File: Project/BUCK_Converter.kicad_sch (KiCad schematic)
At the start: 17 parts, among them J601 Screw_Terminal_01x04, U601 MAX15062AATA+T

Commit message: More files cleanup
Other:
- company: Quasi Peak -> ${COMPANY}
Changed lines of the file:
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@@
     (title "TMC6200-TA-T Eval Board")
     (date "2021-09-03")
-    (rev "ED A0")
-    (company "Quasi Peak")
+    (rev "${REVISION}")
+    (company "${COMPANY}")
+    (comment 1 "${ENGINEER}")
+    (comment 2 "${PHONE_NUMBER}")
+    (comment 3 "${EMAIL}")
+    (comment 4 "${SENTENCE}")
   )
   (junction (at 221.615 80.01) (diameter 0) (color 0 0 0 0)
@@
     (pin "1")
   )
-  (symbol (lib_id "Device:R") (at 168.91 111.76 0) (mirror x)
+  (symbol (lib_id "Device:R") (at 168.91 111.76 0) (mirror x) (unit 1)
     (in_bom yes) (on_board yes)
     (property "Reference" "R603" (id 0) (at 163.195 109.855 0)
@@
     (pin "2")
   )
-  (symbol (lib_id "Device:R") (at 152.4 84.455 0) (mirror x)
+  (symbol (lib_id "Device:R") (at 152.4 84.455 0) (mirror x) (unit 1)
     (in_bom yes) (on_board yes)
     (property "Reference" "R601" (id 0) (at 146.685 82.55 0)
@@
     (pin "2")
   )
-  (symbol (lib_id "Device:R") (at 152.4 93.345 0) (mirror x)
+  (symbol (lib_id "Device:R") (at 152.4 93.345 0) (mirror x) (unit 1)
     (in_bom yes) (on_board yes)
     (property "Reference" "R602" (id 0) (at 146.685 91.44 0)
@@
     (pin "2")
   )
-  (symbol (lib_id "Device:LED") (at 38.1 161.925 90)
+  (symbol (lib_id "Device:LED") (at 38.1 161.925 90) (unit 1)
     (in_bom yes) (on_board yes)
     (property "Reference" "D602" (id 0) (at 32.385 160.655 90)
@@
     (pin "2")
   )
-  (symbol (lib_id "Device:LED") (at 50.8 161.925 90)
+  (symbol (lib_id "Device:LED") (at 50.8 161.925 90) (unit 1)
     (in_bom yes) (on_board yes)
     (property "Reference" "D603" (id 0) (at 45.085 160.655 90)
@@
     (pin "2")
   )
-  (symbol (lib_id "Device:R") (at 38.1 153.035 0) (mirror x)
+  (symbol (lib_id "Device:R") (at 38.1 153.035 0) (mirror x) (unit 1)
     (in_bom yes) (on_board yes)
     (property "Reference" "R605" (id 0) (at 32.385 151.13 0)
@@
     (pin "2")
   )
-  (symbol (lib_id "Device:R") (at 25.4 153.035 0) (mirror x)
+  (symbol (lib_id "Device:R") (at 25.4 153.035 0) (mirror x) (unit 1)
     (in_bom yes) (on_board yes)
     (property "Reference" "R604" (id 0) (at 19.685 151.13 0)
@@
     (pin "2")
   )
-  (symbol (lib_id "Device:R") (at 50.8 153.035 0) (mirror x)
+  (symbol (lib_id "Device:R") (at 50.8 153.035 0) (mirror x) (unit 1)
     (in_bom yes) (on_board yes)
     (property "Reference" "R606" (id 0) (at 45.085 151.13 0)
@@
     (pin "1")
   )
-  (symbol (lib_id "eval_board_tmc6200-ta-rescue:MAX15062BATA+T-eval_board_tmc6200-ta") (at 167.005 77.47 0)
+  (symbol (lib_id "eval_board_tmc6200-ta-rescue:MAX15062BATA+T-eval_board_tmc6200-ta") (at 167.005 77.47 0) (unit 1)
     (in_bom yes) (on_board yes)
     (property "Reference" "U601" (id 0) (at 167.005 76.2 0)
@@
     (pin "1")
   )
-  (symbol (lib_id "Device:C") (at 142.875 89.535 0)
+  (symbol (lib_id "Device:C") (at 142.875 89.535 0) (unit 1)
     (in_bom yes) (on_board yes)
     (property "Reference" "C603" (id 0) (at 137.16 87.63 0)
@@
     (pin "2")
   )
-  (symbol (lib_id "Device:C") (at 120.65 89.535 0)
+  (symbol (lib_id "Device:C") (at 120.65 89.535 0) (unit 1)
     (in_bom yes) (on_board yes)
     (property "Reference" "C602" (id 0) (at 114.935 87.63 0)
@@
     (pin "1")
   )
-  (symbol (lib_id "Device:C") (at 204.47 98.425 0)
+  (symbol (lib_id "Device:C") (at 204.47 98.425 0) (unit 1)
     (in_bom yes) (on_board yes)
     (property "Reference" "C604" (id 0) (at 198.755 96.52 0)
@@
     (pin "1")
   )
-  (symbol (lib_id "Device:C") (at 221.615 88.9 0)
+  (symbol (lib_id "Device:C") (at 221.615 88.9 0) (unit 1)
     (in_bom yes) (on_board yes)
     (property "Reference" "C601" (id 0) (at 215.9 86.995 0)
@@
     (pin "1")
   )
-  (symbol (lib_id "power:+36V") (at 120.65 78.74 0)
+  (symbol (lib_id "power:+36V") (at 120.65 78.74 0) (unit 1)
     (in_bom yes) (on_board yes)
     (property "Reference" "#PWR0603" (id 0) (at 120.65 82.55 0)
@@
     (pin "1")
   )
-  (symbol (lib_id "power:+3.3V") (at 221.615 78.74 0)
+  (symbol (lib_id "power:+3.3V") (at 221.615 78.74 0) (unit 1)
     (in_bom yes) (on_board yes)
     (property "Reference" "#PWR0604" (id 0) (at 221.615 82.55 0)
@@
     (pin "1")
   )
-  (symbol (lib_id "power:GND") (at 25.4 167.005 0)
+  (symbol (lib_id "power:GND") (at 25.4 167.005 0) (unit 1)
     (in_bom yes) (on_board yes)
     (property "Reference" "#PWR0617" (id 0) (at 25.4 173.355 0)
@@
     (pin "1")
   )
-  (symbol (lib_id "Device:LED") (at 25.4 161.925 90)
+  (symbol (lib_id "Device:LED") (at 25.4 161.925 90) (unit 1)
     (in_bom yes) (on_board yes)
     (property "Reference" "D601" (id 0) (at 19.685 160.655 90)
@@
     (pin "2")
   )
-  (symbol (lib_id "power:GND") (at 38.1 167.005 0)
+  (symbol (lib_id "power:GND") (at 38.1 167.005 0) (unit 1)
     (in_bom yes) (on_board yes)
     (property "Reference" "#PWR0618" (id 0) (at 38.1 173.355 0)
@@
     (pin "1")
   )
-  (symbol (lib_id "power:+3.3V") (at 38.1 147.955 0)
+  (symbol (lib_id "power:+3.3V") (at 38.1 147.955 0) (unit 1)
     (in_bom yes) (on_board yes)
     (property "Reference" "#PWR0615" (id 0) (at 38.1 151.765 0)
@@
     (pin "1")
   )
-  (symbol (lib_id "power:+36V") (at 41.91 58.42 0)
+  (symbol (lib_id "power:+36V") (at 41.91 58.42 0) (unit 1)
     (in_bom yes) (on_board yes)
     (property "Reference" "#PWR0601" (id 0) (at 41.91 62.23 0)
@@
     (pin "1")
   )
-  (symbol (lib_id "power:GND") (at 50.8 167.005 0)
+  (symbol (lib_id "power:GND") (at 50.8 167.005 0) (unit 1)
     (in_bom yes) (on_board yes)
     (property "Reference" "#PWR0619" (id 0) (at 50.8 173.355 0)
@@
     (pin "1")
   )
-  (symbol (lib_id "power:+36V") (at 50.8 147.955 0)
+  (symbol (lib_id "power:+36V") (at 50.8 147.955 0) (unit 1)
     (in_bom yes) (on_board yes)
     (property "Reference" "#PWR0616" (id 0) (at 50.8 151.765 0)

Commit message: Cleanup ED A1 version
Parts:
- FB601: symbol Device:Ferrite_Bead -> Device:FerriteBead_Small
- U601: symbol eval_board_tmc6200-ta-rescue:MAX15062BATA+T-eval_board_tmc6200-ta -> QP_LIBRARY:MAX15062BATA+T
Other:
- moved on the sheet: D601, D602, D603, R604, R605, R606

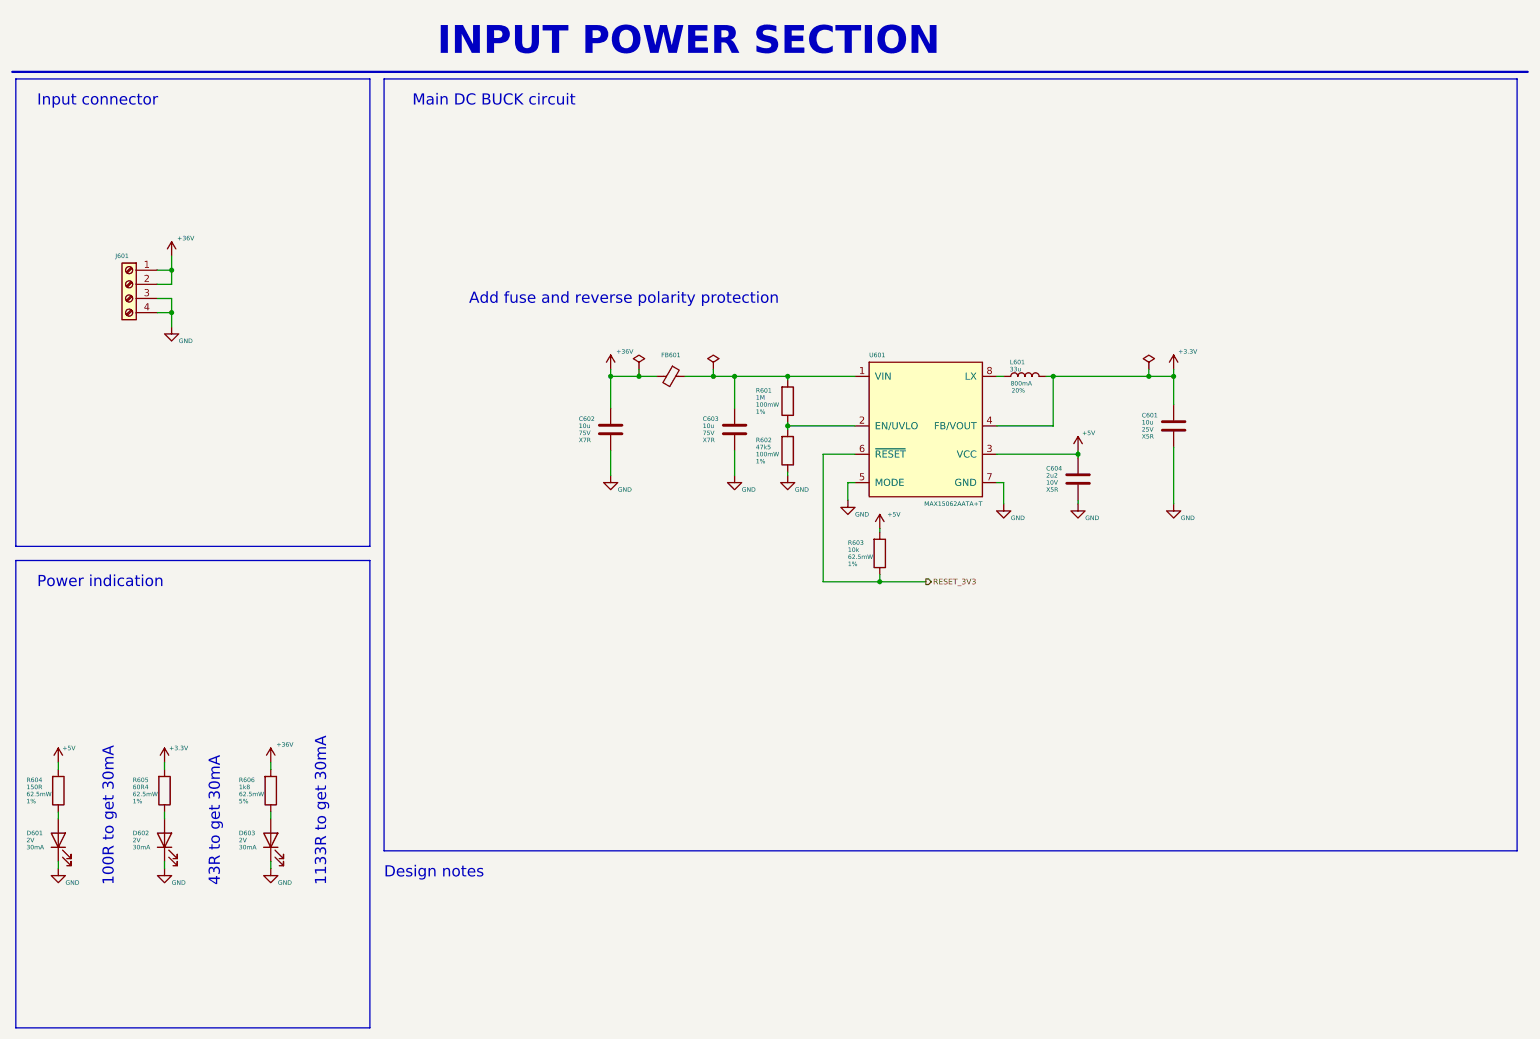
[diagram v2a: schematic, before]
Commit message: Cleaning files, added testpoints
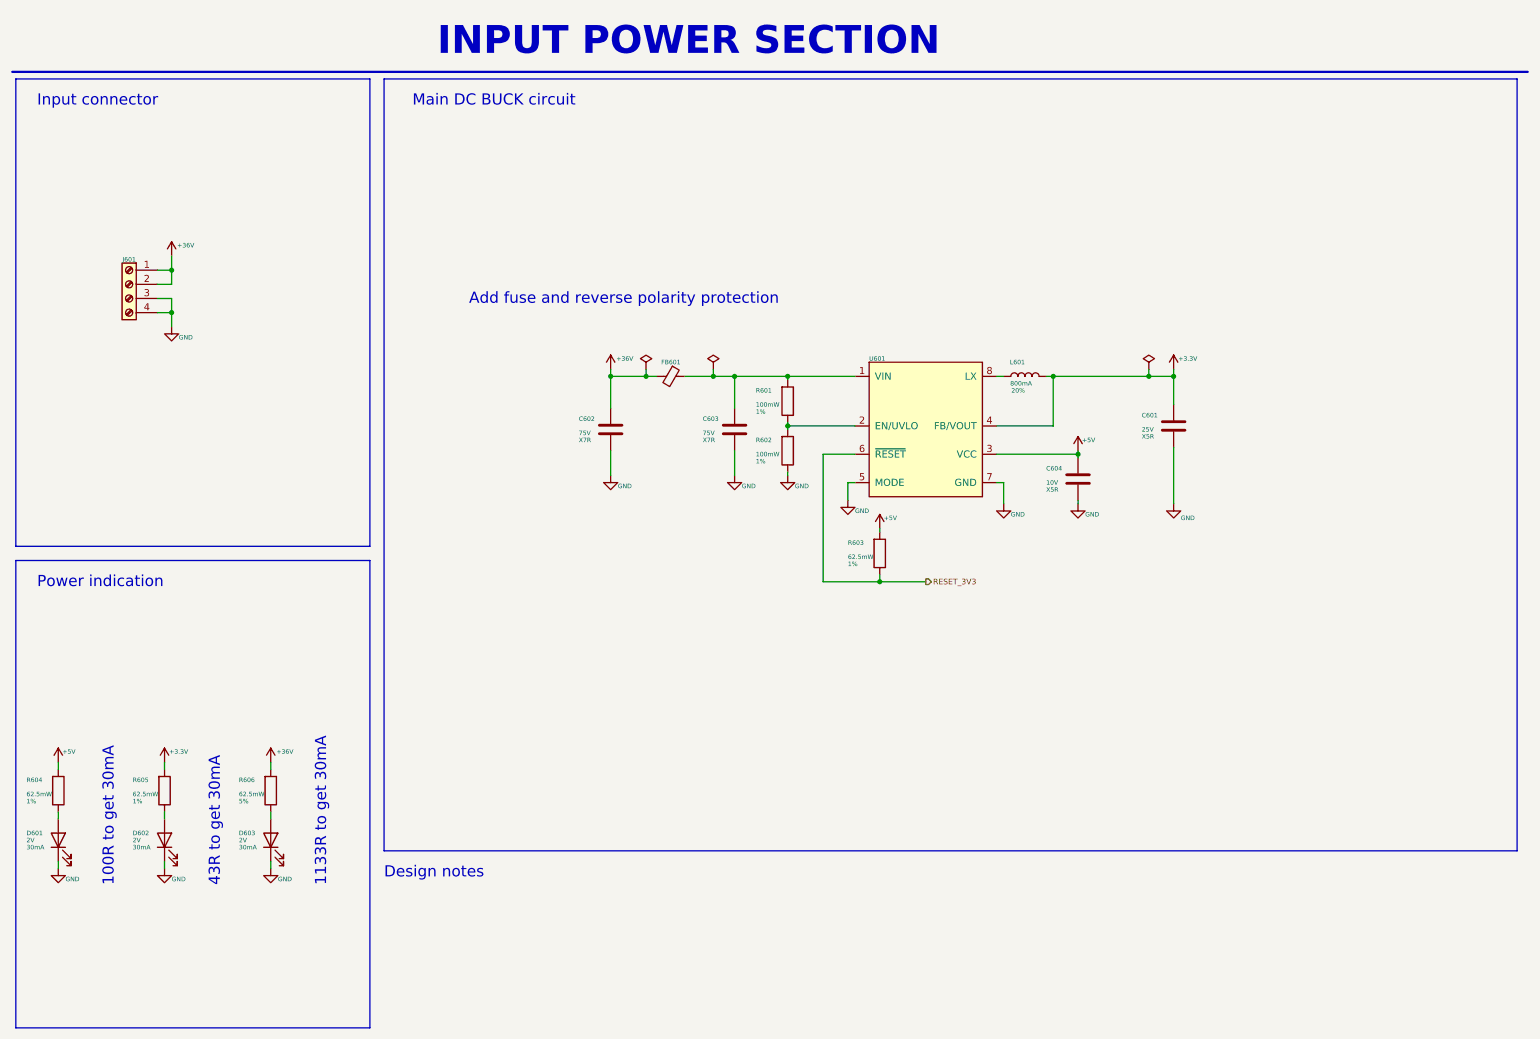
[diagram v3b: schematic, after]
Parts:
- C601: value 10u -> (none); footprint Capacitor_SMD:C_1206_3216Metric -> (none)
- C602, C603: value 10u -> (none); footprint Capacitor_SMD:C_1210_3225Metric -> (none)
- C604: value 2u2 -> (none); footprint Capacitor_SMD:C_0603_1608Metric -> (none)
- D601, D602, D603: value LED -> (none); footprint Diode_SMD:D_0402_1005Metric -> (none)
- FB601: value Ferrite_Bead -> (none); footprint Resistor_SMD:R_0603_1608Metric -> (none)
- J601: value Screw_Terminal_01x04 -> (none); footprint Connector_PinSocket_2.54mm:PinSocket_1x04_P2.54mm_Vertical -> (none)
- L601: value 33u -> (none); footprint Inductor_SMD:L_Coilcraft_XAL5030 -> (none)
- R601: value 1M -> (none); footprint Resistor_SMD:R_0603_1608Metric -> (none)
- R602: value 47k5 -> (none); footprint Resistor_SMD:R_0603_1608Metric -> (none)
- R603: value 10k -> (none); footprint Resistor_SMD:R_0402_1005Metric -> (none)
- R604: value 150R -> (none); footprint Resistor_SMD:R_0402_1005Metric -> (none)
- R605: value 60R4 -> (none); footprint Resistor_SMD:R_0402_1005Metric -> (none)
- R606: value 1k8 -> (none); footprint Resistor_SMD:R_0402_1005Metric -> (none)
- U601: value MAX15062AATA+T -> (none); footprint eval_board_tmc6200-ta:MAX15062AATA+T_TDFN-8 -> (none)
